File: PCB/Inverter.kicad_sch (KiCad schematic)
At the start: 79 parts, among them J1 Conn_01x02, J2 Conn_01x05_Pin, J3 Conn_01x05_Pin, Q1 STP110N8F6, Q2 STP110N8F6, Q3 STP110N8F6, Q4 STP110N8F6, Q5 STP110N8F6, Q6 STP110N8F6, U1 XL7015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

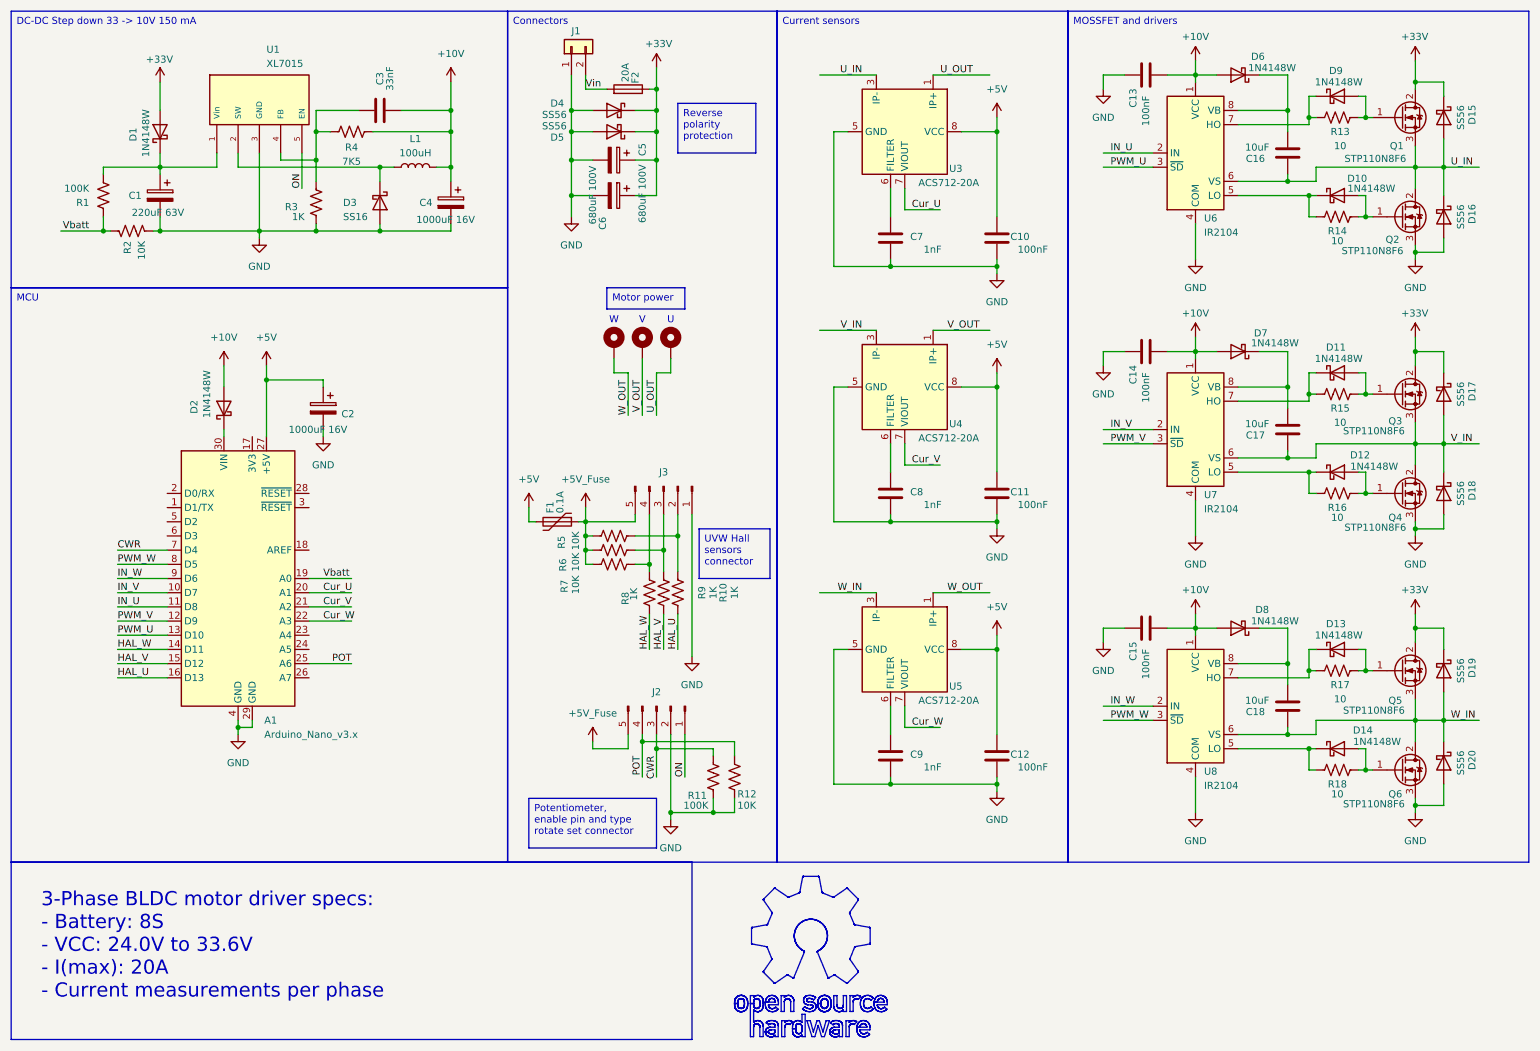
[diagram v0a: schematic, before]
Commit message: Change#009
Changed the pin on phase W from 5 to 3 (so that all PWMs are at the same frequency);
Added a thermal barrier for all components on the negative side to make it easier to assemble the device;
Changed the size of the board, it became a little larger (to increase the ground current);
Added frames for connectors with a description in the diagram for a better understanding of which connector is for what.
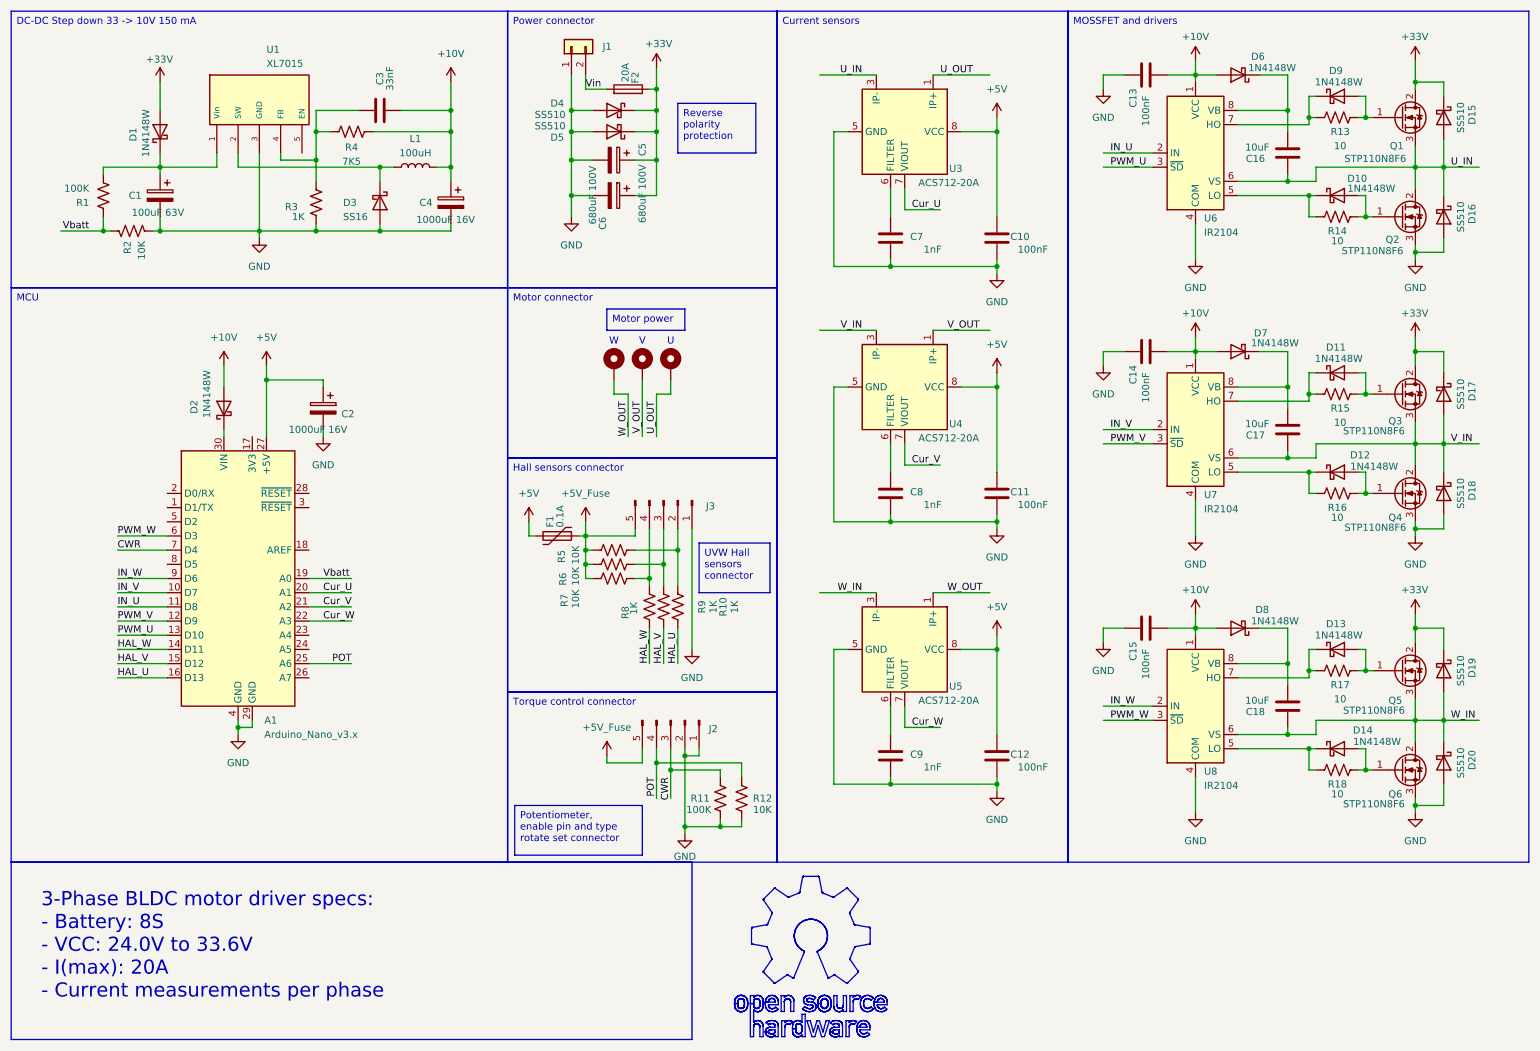
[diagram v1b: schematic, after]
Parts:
- C1: value 220uF 63V -> 100uF 63V
- C2, C4: footprint Capacitor_SMD:CP_Elec_8x10.5 -> Capacitor_SMD:CP_Elec_10x10.5
- D15, D16, D17, D18, D19, D20, D4, D5: value SS56 -> SS510
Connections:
- net GND: now also J2.1 (Pin_1)
- net PWM_W: now also A1.6 (D3); no longer A1.8 (D5)
- net ON: no longer names the net of U1.5 (EN)
- net ON: no longer J2.1 (Pin_1)
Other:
- moved on the sheet: F1, J2, J3, R10, R11, R12, R5, R6, R7, R8, R9
